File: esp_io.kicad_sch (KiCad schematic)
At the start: 0 parts

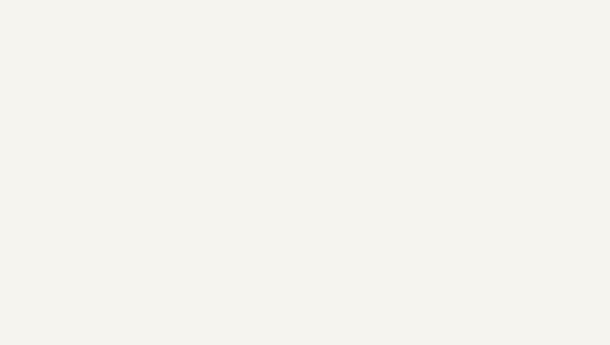
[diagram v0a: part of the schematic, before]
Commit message: schematic: add project structure wiring
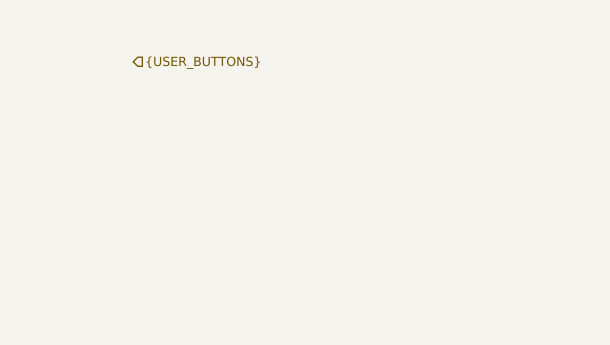
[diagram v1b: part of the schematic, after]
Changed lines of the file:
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@@
+		)
+	)
+	(hierarchical_label "{USER_BUTTONS}"
+		(shape input)
+		(at 46.99 71.12 0)
+		(effects
+			(font
+				(size 1.016 1.016)
+			)
+			(justify left)
 		)
 	)

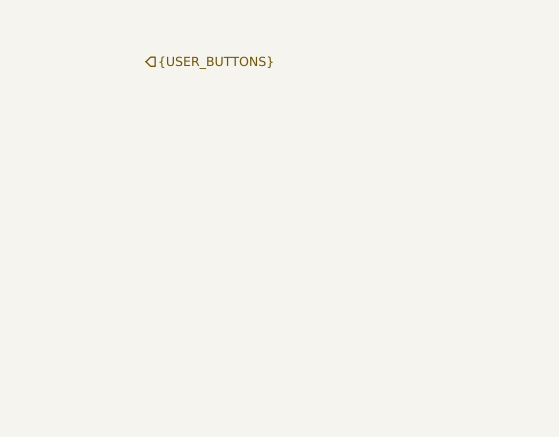
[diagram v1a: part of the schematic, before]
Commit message: Add power stages
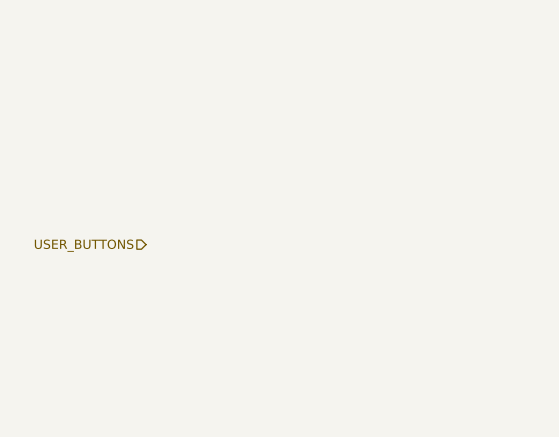
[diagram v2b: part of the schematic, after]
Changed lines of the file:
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@@
 		)
 	)
-	(hierarchical_label "{USER_BUTTONS}"
+	(hierarchical_label "USER_BUTTONS"
 		(shape input)
-		(at 46.99 71.12 0)
+		(at 46.99 91.44 180)
 		(effects
 			(font
 				(size 1.016 1.016)
 			)
-			(justify left)
+			(justify right)
 		)
 	)

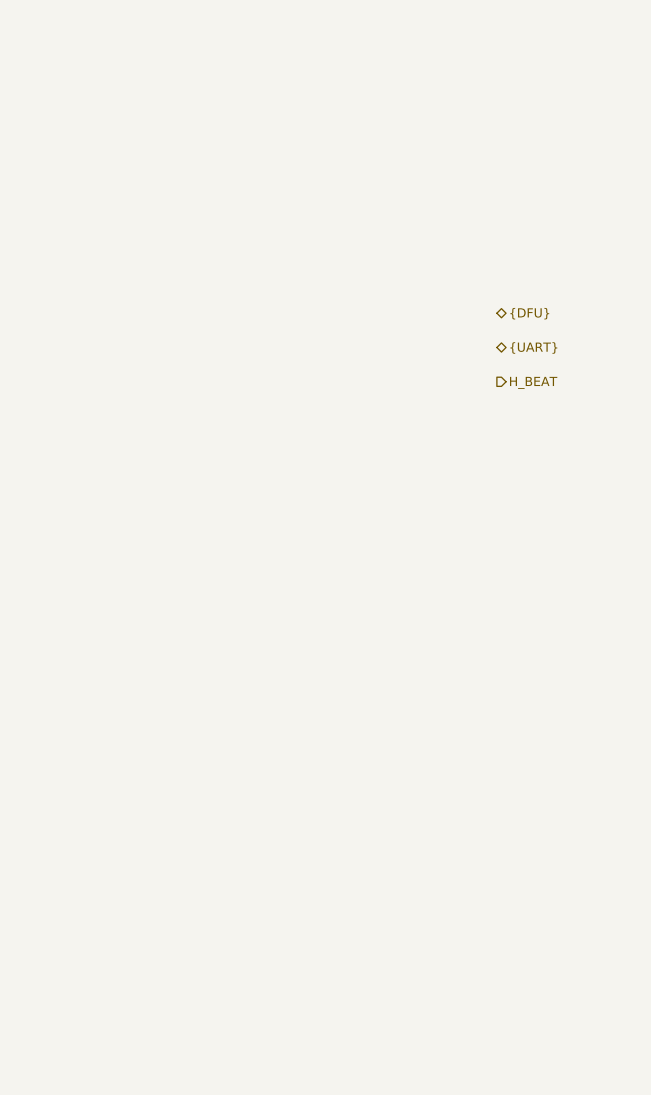
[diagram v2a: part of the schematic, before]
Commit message: Remove STM
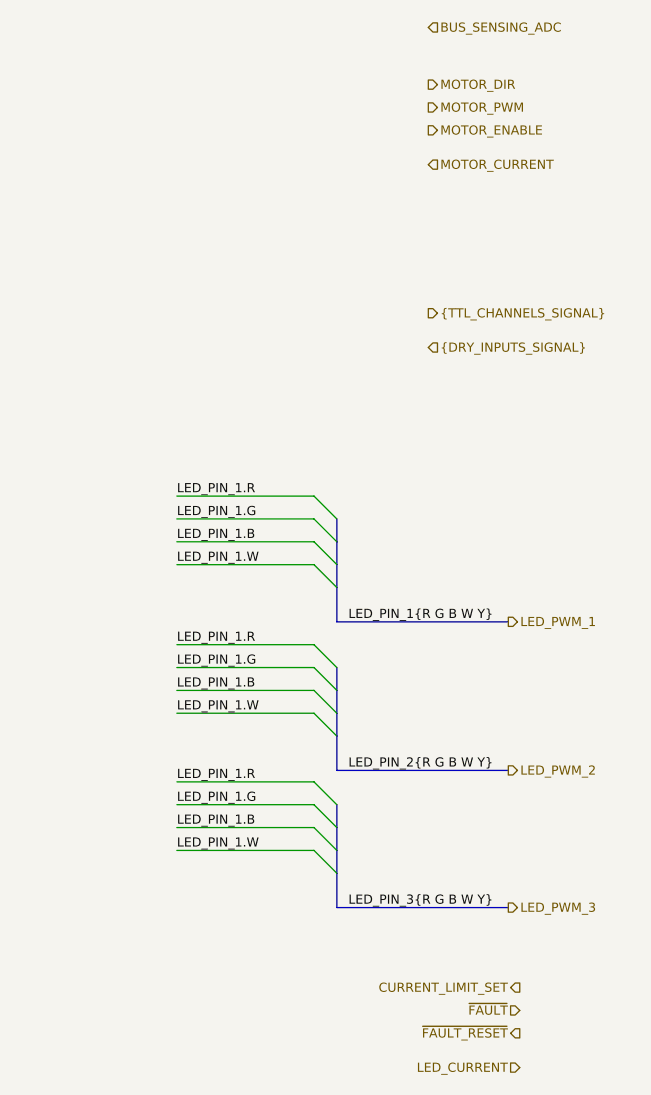
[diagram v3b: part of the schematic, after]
